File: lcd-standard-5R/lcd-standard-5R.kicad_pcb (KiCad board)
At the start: 4 copper layers, 137.4 x 82.6 mm, 172 parts, among them J1 USB_C_Receptacle_USB2.0_16P, J10 CTP_10P, J2 SWD, J3 Conn_ARM_JTAG_SWD_10, J4 Micro_SD_Card_Det1, J5 CTP_6P, J6 LCD_40P, J7 Conn_01x02_MountingPin, J8 Serial, J9 AUX_IO, Q1 DMG3415, Q2 MMBT3904, Q3 MMBT3904, Q4 MMBT3904, SW1 SW_Push, SW2 SW_Push, SW3 BOOT0, SW4 RST, U1 USBLC6-2SC6, U2 AMS1117-3.3, U3 STM32H743ZITx, U4 MT48LC16M16A2P, U5 MT25Q, U6 CAT24C256, U7 XPT2046TS, U8 TPS61169, U9 MAX98357A, Y1 25MHz, Y2 32.768KHz

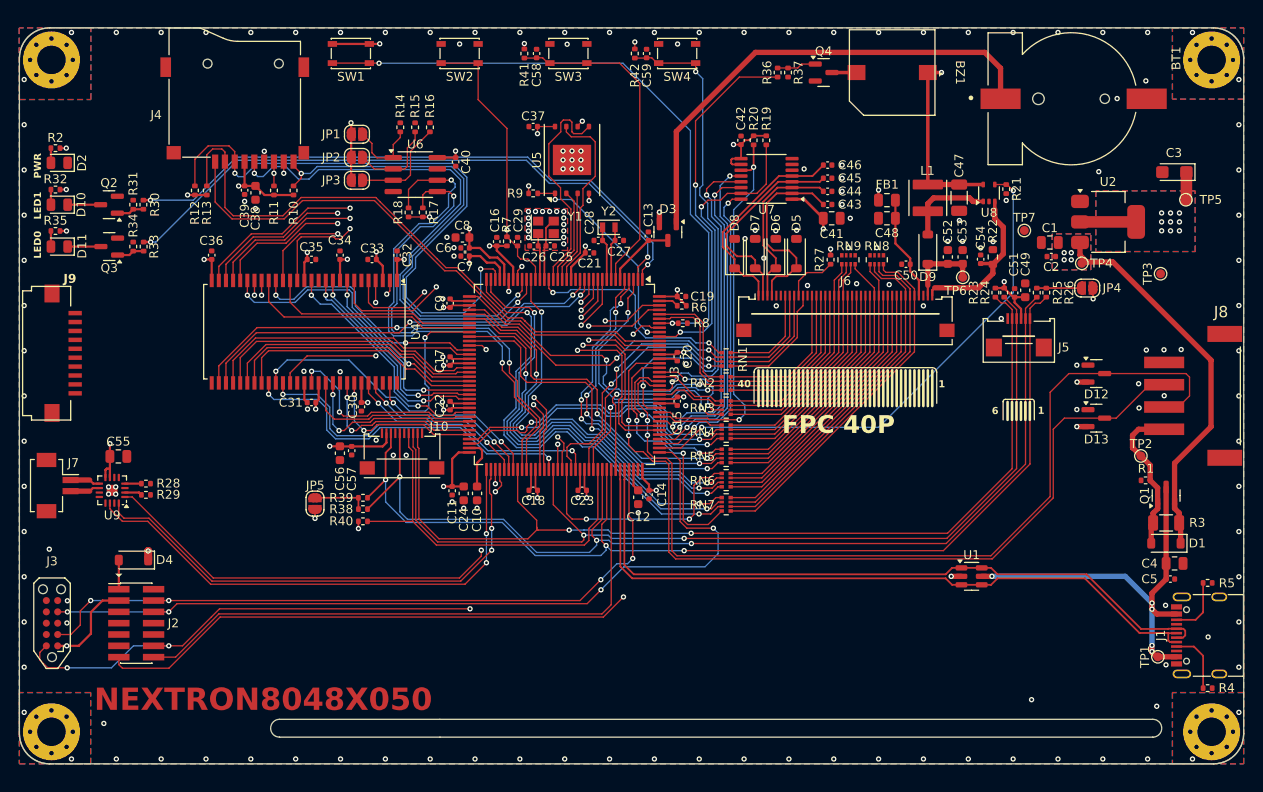
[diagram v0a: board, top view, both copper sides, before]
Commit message: Adding filter on MAX98357, TODO: Add more grounding vias
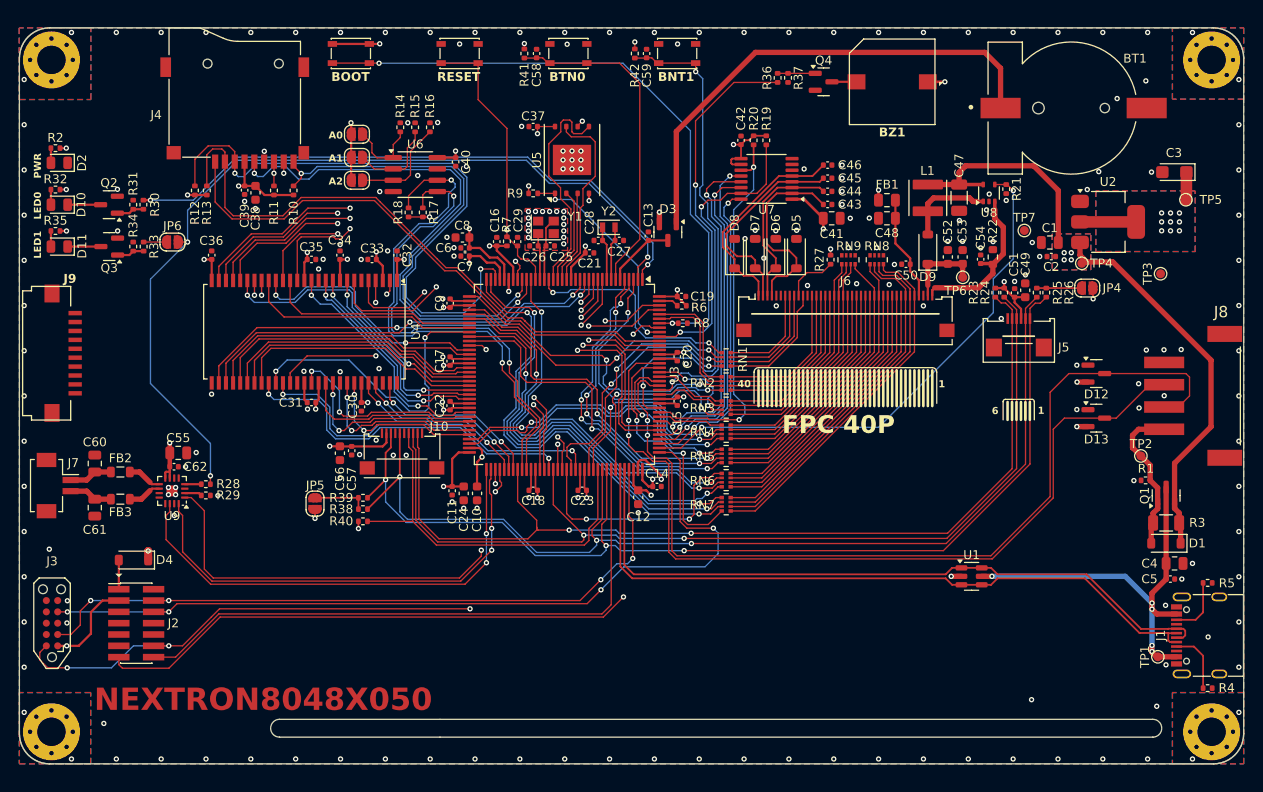
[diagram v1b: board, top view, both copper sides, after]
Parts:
- added C60: 220pF, Capacitor_SMD:C_0805_2012Metric, F.Cu at (84.9, 102.8)
- added C61: 220pF, Capacitor_SMD:C_0805_2012Metric, F.Cu at (84.9, 107.8)
- added C62: 100n, Capacitor_SMD:C_0402_1005Metric, F.Cu at (93.8, 103.2)
- added FB2: FerriteBead, Inductor_SMD:L_0805_2012Metric, F.Cu at (87.8, 103.8)
- added FB3: FerriteBead, Inductor_SMD:L_0805_2012Metric, F.Cu at (87.8, 106.8)
- added JP6: JMP, Jumper:SolderJumper-2_P1.3mm_Open_RoundedPad1.0x1.5mm, F.Cu at (93.6, 78.0)
- moved C55 6.73 mm to (94.3, 101.6)
- moved R28 6.72 mm to (97.3, 105.1)
- moved R29 6.72 mm to (97.3, 106.4)
- moved U9 6.72 mm to (93.6, 105.9)
- moved C14 1.28 mm to (148.0, 105.4), turned to 0 degrees
- moved BZ1 1.04 mm to (174.4, 60.0)
- moved Q4 1.04 mm to (166.7, 60.0)
- moved BT1 1.04 mm to (194.5, 62.9)
- moved R36 0.60 mm to (161.5, 59.5)
- moved R37 0.60 mm to (162.7, 59.5)
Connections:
- R33 pad 1: /IO/LED1 -> Net-(JP6-A)
- U3 pad 2: /IO/LED1 -> /OUTPUT_SPEAKER/~{SD_MODE}
- U9 pad 10: Net-(J7-Pin_2) -> Net-(U9-OUTN)
- U9 pad 9: Net-(J7-Pin_1) -> Net-(U9-OUTP)
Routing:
- net /OUTPUT_SPEAKER/~{SD_MODE}: track 0.00 -> 98.7 mm, vias 0 -> 3
- net /IO/LED1: track 68.8 -> 0.00 mm, vias 2 -> 0
- net /OUTPUT_SPEAKER/I2S2_SDO: track 84.3 -> 134.0 mm
- net /MCU/NRST: track 135.7 -> 185.3 mm
- net Net-(C10-Pad1): track 8.38 -> 31.1 mm, vias 0 -> 2
- net VDD: track 240.6 -> 249.2 mm
- net GND: track 21.5 -> 26.1 mm, vias 184 -> 219
- net /OUTPUT_SPEAKER/I2S2_CLK: track 56.8 -> 52.3 mm
- net /OUTPUT_SPEAKER/I2S2_WS: track 57.9 -> 53.7 mm
- net Net-(U9-OUTP): track 0.00 -> 3.86 mm
- net Net-(U9-OUTN): track 0.00 -> 3.78 mm
- net /MCU/SD_D1: track 70.5 -> 67.7 mm
- net Net-(JP6-A): track 0.00 -> 2.58 mm
- net /MCU/SD_D0: track 72.8 -> 70.3 mm
- net /MCU/SDRAM_DQ1: track 38.8 -> 40.6 mm
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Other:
- board text added: "A0"
- board text added: "A1"
- board text added: "A2"
- board text added: "BNT1"
- board text added: "BOOT"
- board text added: "BTN0"
- board text added: "RESET"

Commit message: Added 3.4inch bar LCD to the dimension
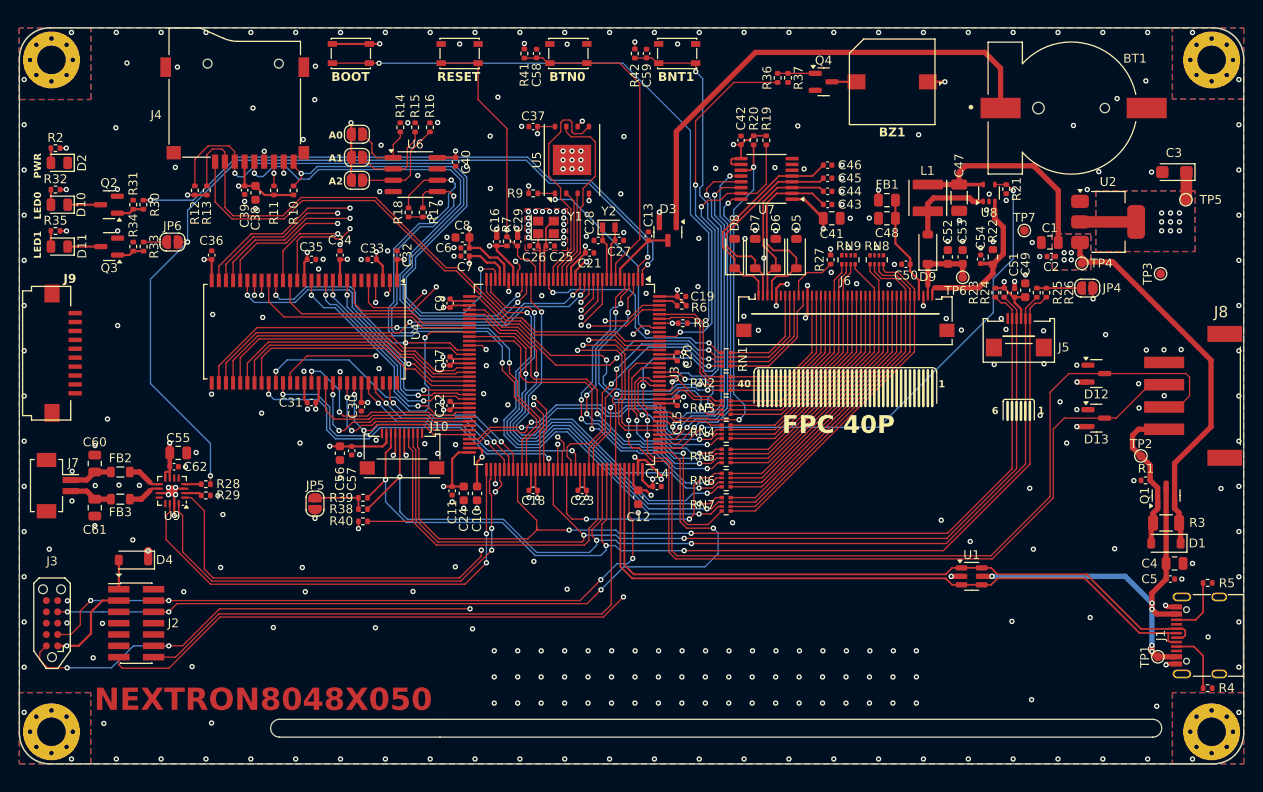
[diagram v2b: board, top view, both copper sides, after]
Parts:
- C60, C61: value 220pF -> 220p
- FB2, FB3: value FerriteBead -> 600
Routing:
- net GND: track 26.1 -> 52.8 mm, vias 219 -> 367

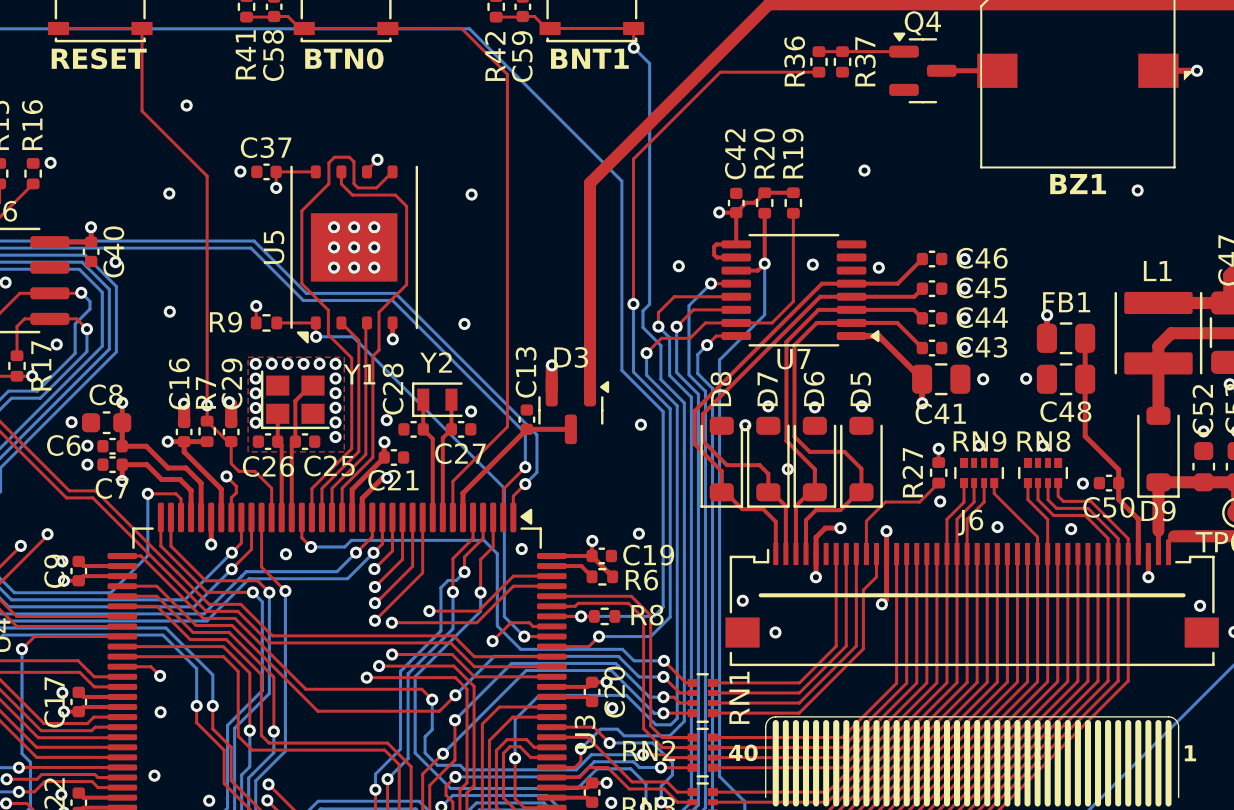
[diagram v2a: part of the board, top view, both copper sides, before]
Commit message: Add QSPI Flash trace length matching to 5 inch LCD
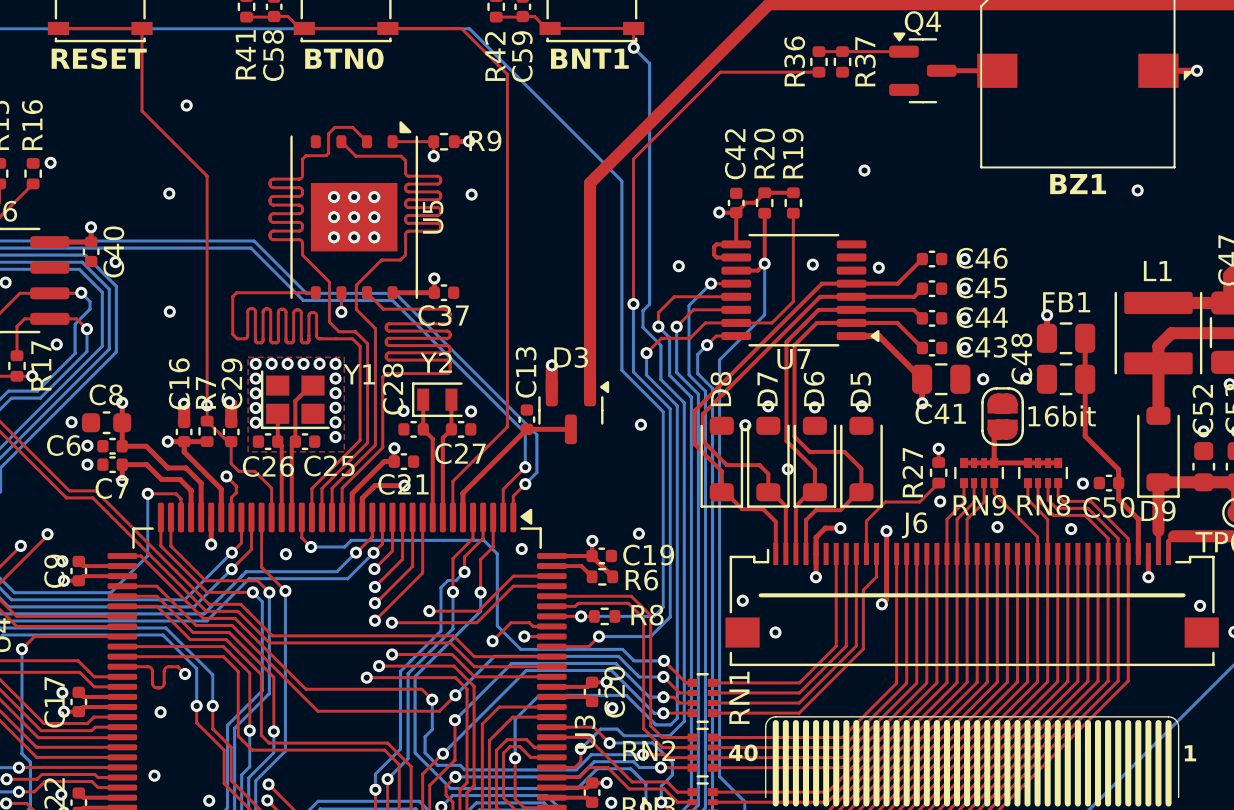
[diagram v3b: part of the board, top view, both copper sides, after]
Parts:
- added 16bit: JMP, Jumper:SolderJumper-2_P1.3mm_Open_RoundedPad1.0x1.5mm, F.Cu at (170.6, 77.1)
- moved R9 12.6 mm to (142.9, 63.5), turned to 180 degrees
- moved C37 10.7 mm to (142.9, 71.0), turned to 0 degrees
- moved U5 1.50 mm to (138.4, 67.2), turned to -90 degrees
- moved C21 0.54 mm to (140.9, 79.4)
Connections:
- RN8 pad 5: GND -> Net-(JP8-B)
- RN8 pad 6: GND -> Net-(JP8-B)
- RN8 pad 7: GND -> Net-(JP8-B)
- RN8 pad 8: GND -> Net-(JP8-B)
- RN9 pad 5: GND -> Net-(JP8-B)
- RN9 pad 6: GND -> Net-(JP8-B)
- RN9 pad 7: GND -> Net-(JP8-B)
- RN9 pad 8: GND -> Net-(JP8-B)
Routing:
- net /MEMORY_FLASH/NOR_IO2: track 10.4 -> 36.9 mm
- net /MEMORY_FLASH/NOR_DO(IO1): track 10.8 -> 36.9 mm
- net /MEMORY_FLASH/NOR_IO3: track 21.1 -> 37.0 mm
- net /MEMORY_FLASH/~{NOR_CS}: track 24.2 -> 38.7 mm
- net /MEMORY_FLASH/NOR_DI(IO0): track 24.9 -> 36.9 mm
- net Net-(JP8-B): track 0.00 -> 6.50 mm
- net /MEMORY_FLASH/NOR_CLK: track 42.1 -> 36.7 mm
- net GND: track 52.8 -> 52.7 mm, vias 367 -> 362

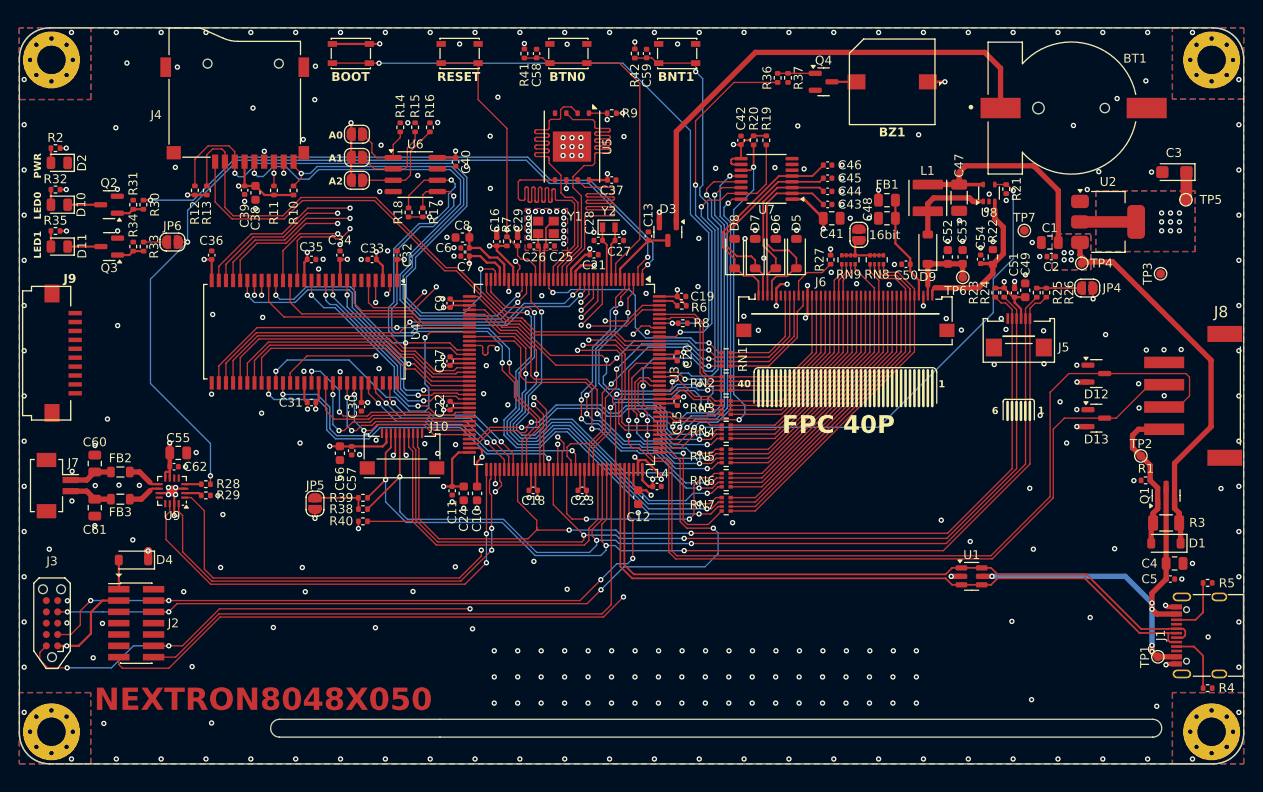
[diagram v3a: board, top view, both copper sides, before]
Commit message: Change standoff dimension to match TJC LCD
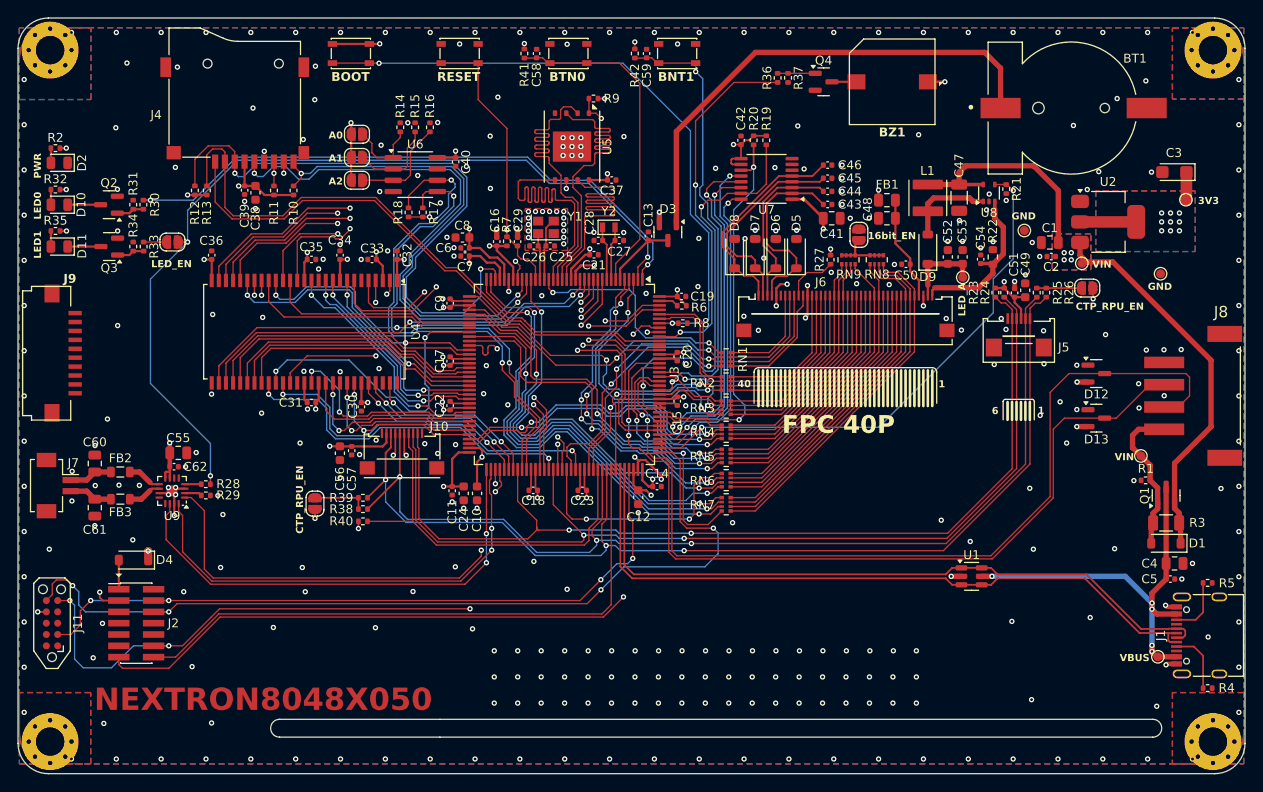
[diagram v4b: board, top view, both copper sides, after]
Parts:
- removed J3: Conn_ARM_JTAG_SWD_10, Connector:Tag-Connect_TC2050-IDC-NL_2x05_P1.27mm_Vertical
- added J11: TAG_CONNECT, Connector:Tag-Connect_TC2050-IDC-NL_2x05_P1.27mm_Vertical, F.Cu at (80.1, 120.7)
- moved R9 2.62 mm to (140.9, 61.8)
- moved H1 1.11 mm to (79.9, 56.4)
- moved H2 1.11 mm to (79.9, 134.0)
- moved H3 1.11 mm to (210.4, 56.4)
- moved H4 1.11 mm to (210.4, 134.0)
- renumbered 16bit to JP8
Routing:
- net +3V3: track 177.2 -> 170.7 mm, vias 56 -> 57
- net /MCU/SWCLK: track 95.2 -> 100.5 mm
- net /MCU/NRST: track 185.3 -> 187.7 mm
- net GND: vias 362 -> 360
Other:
- board size 137.4 x 82.6 mm -> 137.7 x 84.8 mm
- board text added: "16bit_EN"
- board text added: "3V3"
- board text added: "CTP_RPU_EN"
- board text added: "GND"
- board text added: "LED_A"
- board text added: "LED_EN"
- board text added: "VBUS"
- board text added: "VIN"
